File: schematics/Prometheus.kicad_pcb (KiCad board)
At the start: 2 copper layers, 170.2 x 170.2 mm, 127 parts, among them J1 ATX Power Conn, J10 Centronics, J11 ps/2 keyb, J12 Expansion, J13 Joy1, J14 Joy2, J15 rs232, J16 DIN41612_02x32_AB, J17 DIN41612_02x32_AB, J18 SPEAKER, J2 FDC Connector, J3 IDE Connector, J4 JTAG, J5 Left Audio, J6 Right Audio, J7 GRACE board interface 1, J8 GRACE board interface 2, J9 15kHz Video Out, SW1 Power Switch, SW2 Reset Switch, U1 DS1501YN, U10 2764, U11 EN5503DOC, U12 VRAM, U13 wdc65c22, U14 wdc65c51, U15 MAX233CPP, U16 wdc65c22, U17 41464, U18 41464, U19 41464, U2 wdc65c816, U20 41464, U21 SIMM16M, U22 SIMM16M, U23 SIMM16M, U3 WD1772, U8 XC9572XL-TQ100, U9 SIMM16M, X1 32kHz, X2 8MHz, X3 1.8432MHz

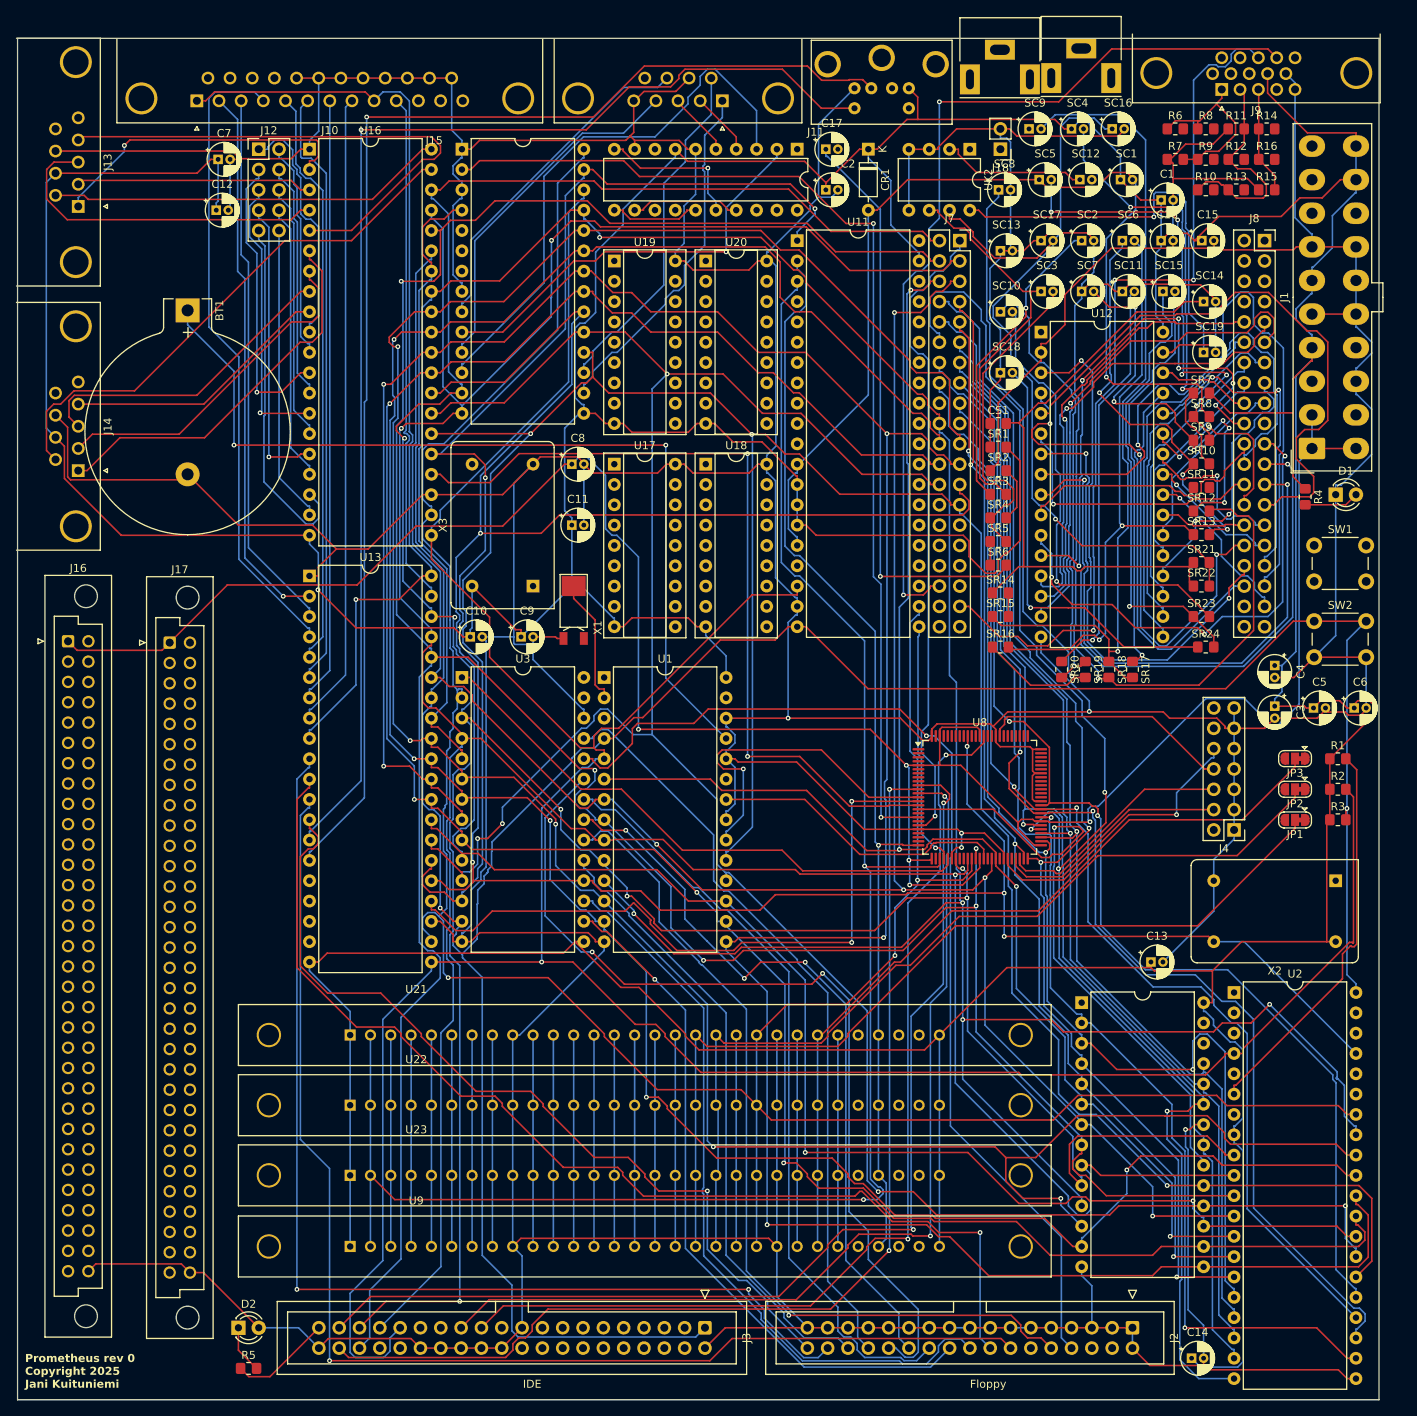
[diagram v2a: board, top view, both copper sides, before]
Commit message: Added the rest of the footprints for the analog audio and re-did the layout and routing of the PCB.
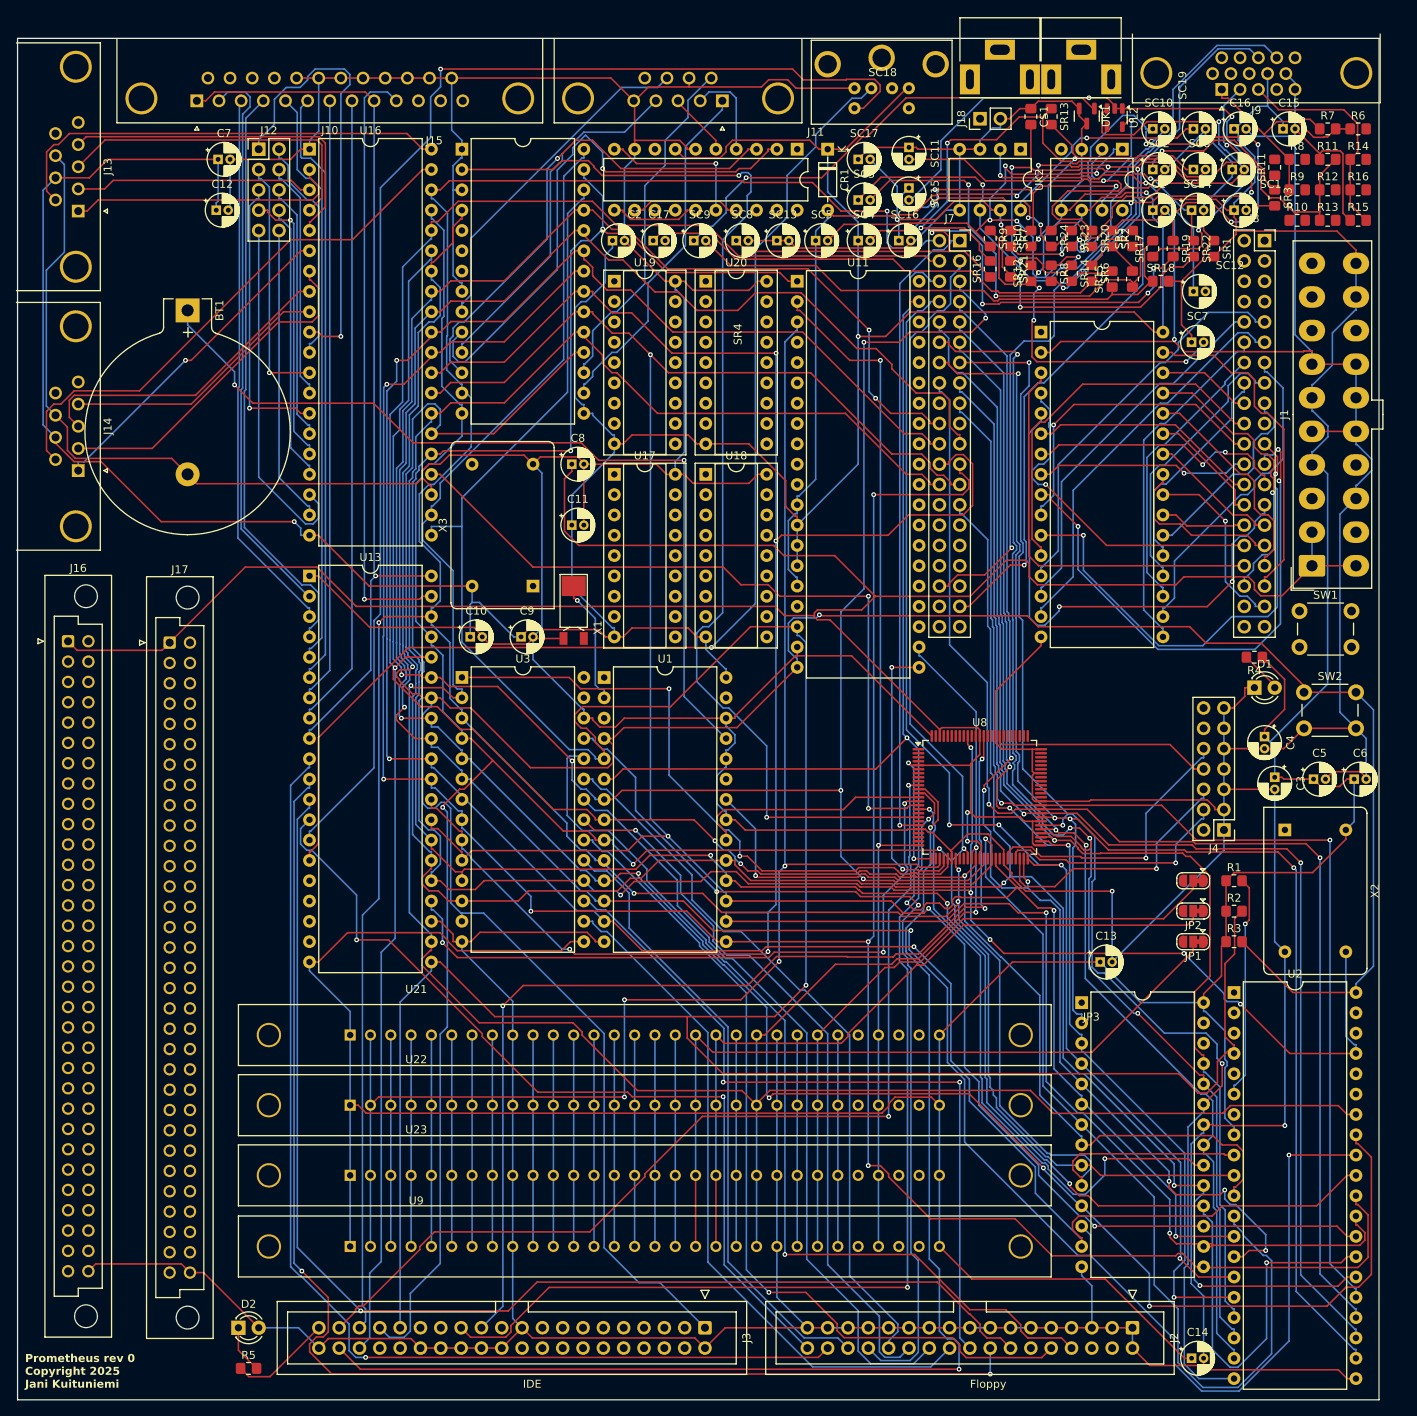
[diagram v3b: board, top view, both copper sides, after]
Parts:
- added UK1: LM3340, Package_TO_SOT_SMD:SOT-23, F.Cu at (241.9, 27.6)
- added UL1: MC34084, Package_DIP:DIP-8_W7.62mm, F.Cu at (246.4, 31.8)
- added UL2: TL072, Package_TO_SOT_SMD:SOT-23-5, F.Cu at (245.4, 27.8)
- moved SR13 55.5 mm to (237.5, 27.7), turned to -90 degrees
- moved SR24 54.6 mm to (237.5, 42.9), turned to -90 degrees
- moved SR20 54.0 mm to (242.6, 42.9)
- moved SR19 53.7 mm to (252.7, 44.2)
- moved SR17 52.7 mm to (250.2, 44.2), turned to 90 degrees
- moved SR3 50.7 mm to (265.4, 37.8), turned to -90 degrees
- moved SR23 50.0 mm to (240.0, 42.9), turned to -90 degrees
- moved SR18 49.0 mm to (251.2, 48.3), turned to 0 degrees
- moved SR16 47.3 mm to (229.9, 46.7), turned to 90 degrees
- moved SR15 44.4 mm to (245.1, 48.0), turned to 90 degrees
- moved SC9 44.2 mm to (192.8, 43.2)
- moved SR21 43.8 mm to (232.4, 46.7), turned to -90 degrees
- moved SR22 42.2 mm to (255.3, 44.2), turned to -90 degrees
- moved SR5 41.4 mm to (247.7, 42.9), turned to 90 degrees
- moved SR11 41.0 mm to (265.4, 34.0), turned to 90 degrees
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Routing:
- net GNDA: track 217.5 -> 150.1 mm
- net Net-(SC9-Pad1): track 0.00 -> 59.1 mm, vias 0 -> 1
- net A3: track 286.3 -> 341.3 mm, vias 5 -> 7
- net Net-(J8-Pin_25): track 78.2 -> 32.9 mm
- net D4: track 297.6 -> 340.0 mm, vias 4 -> 6
- net +12V: track 105.4 -> 65.0 mm, vias 1 -> 4
- net D0: track 363.0 -> 323.4 mm, vias 5 -> 7
- net Net-(SC9-Pad2): track 104.4 -> 66.8 mm, vias 1 -> 0
- net D7: track 342.6 -> 306.3 mm
- net Net-(UL2B--): track 57.6 -> 23.5 mm
- net Net-(J8-Pin_24): track 60.3 -> 26.7 mm
- net A12: track 163.3 -> 194.4 mm, vias 2 -> 4
- net CAS: track 223.2 -> 193.5 mm, vias 2 -> 4
- net GND: track 1218.1 -> 1246.6 mm, vias 5 -> 4
- net D3: track 357.9 -> 330.5 mm, vias 5 -> 6
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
